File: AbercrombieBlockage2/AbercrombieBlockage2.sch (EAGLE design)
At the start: 35 parts, among them U1 DMN3135LVT, U2 ICS-43434, U3 CYBLE-022001-00, U4 LIS3DH, U5 VL53L0X, U6 VL53L0X, U7 VL53L0X, U8 M24

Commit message: Starting to change the Abercrombie blockage 2 design.
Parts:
- BAT1: DIGIKEY (none) -> BK-913-ND
- C1: DIGIKEYY (none) -> 490-13250-1-ND
- LED1: DIGIKEY (none) -> 160-2162-1-ND
- SV2: DIGIKEY (none) -> 952-2246-ND
- U8: DIGIKEY 497-6348-1-ND -> 497-6351-1-ND
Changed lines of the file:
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@@
 </classes>
 <parts>
-<part name="C1" library="resistor" deviceset="C-US" device="C1210" value="220u"/>
+<part name="C1" library="resistor" deviceset="C-US" device="C1210" value="220u">
+<attribute name="DIGIKEYY" value="490-13250-1-ND"/>
+</part>
 <part name="U1" library="NicksParts" deviceset="DMN3135LVT" device="">
 <attribute name="DIGIKEY" value="DMN3135LVT-7DICT-ND"/>
@@
 <part name="C4" library="resistor" deviceset="C-US" device="C1210" value="10u"/>
 <part name="C3" library="resistor" deviceset="C-US" device="C0603" value="1u"/>
-<part name="SV2" library="con-lstb" deviceset="MA05-1" device=""/>
-<part name="LED1" library="NicksParts" deviceset="LTST-C19HE1WT" device=""/>
+<part name="SV2" library="con-lstb" deviceset="MA05-1" device="">
+<attribute name="DIGIKEY" value="952-2246-ND"/>
+</part>
+<part name="LED1" library="NicksParts" deviceset="LTST-C19HE1WT" device="">
+<attribute name="DIGIKEY" value="160-2162-1-ND"/>
+</part>
 <part name="R2" library="resistor" deviceset="R-US_" device="R0603" value="360"/>
 <part name="U3" library="NicksParts" deviceset="CYBLE-022001-00" device="">
@@
 </part>
 <part name="U8" library="NicksParts" deviceset="M24" device="">
-<attribute name="DIGIKEY" value="497-6348-1-ND"/>
+<attribute name="DIGIKEY" value="497-6351-1-ND"/>
 </part>
 <part name="U4" library="NicksParts" deviceset="LIS3DH" device="">
@@
 <part name="SUPPLY13" library="supply2" deviceset="V+" device=""/>
 <part name="R5" library="resistor" deviceset="R-US_" device="R0603" value="360"/>
-<part name="BAT1" library="NicksParts" deviceset="SN2032" device=""/>
+<part name="BAT1" library="NicksParts" deviceset="SN2032" device="">
+<attribute name="DIGIKEY" value="BK-913-ND"/>
+</part>
 <part name="TX" library="testpad" deviceset="TP" device="B1,27"/>
 <part name="GND" library="testpad" deviceset="TP" device="B1,27"/>
@@
 </plain>
 <instances>
-<instance part="C1" gate="G$1" x="17.78" y="71.12"/>
+<instance part="C1" gate="G$1" x="17.78" y="71.12">
+<attribute name="DIGIKEYY" x="17.78" y="71.12" size="1.778" layer="96" display="off"/>
+</instance>
 <instance part="U1" gate="G$1" x="20.32" y="17.78">
 <attribute name="DIGIKEY" x="20.32" y="17.78" size="1.778" layer="96" display="off"/>
@@
 <instance part="C4" gate="G$1" x="40.64" y="71.12"/>
 <instance part="C3" gate="G$1" x="30.48" y="71.12"/>
-<instance part="SV2" gate="G$1" x="-10.16" y="106.68"/>
-<instance part="LED1" gate="G$1" x="106.68" y="25.4"/>
+<instance part="SV2" gate="G$1" x="-10.16" y="106.68">
+<attribute name="DIGIKEY" x="-10.16" y="106.68" size="1.778" layer="96" display="off"/>
+</instance>
+<instance part="LED1" gate="G$1" x="106.68" y="25.4">
+<attribute name="DIGIKEY" x="106.68" y="25.4" size="1.778" layer="96" display="off"/>
+</instance>
 <instance part="R2" gate="G$1" x="111.76" y="10.16" rot="R270"/>
 <instance part="U3" gate="G$1" x="99.06" y="96.52">
@@
 <instance part="SUPPLY13" gate="1" x="101.6" y="35.56"/>
 <instance part="R5" gate="G$1" x="106.68" y="10.16" rot="R270"/>
-<instance part="BAT1" gate="1" x="0" y="63.5" rot="R90"/>
+<instance part="BAT1" gate="1" x="0" y="63.5" rot="R90">
+<attribute name="DIGIKEY" x="0" y="63.5" size="1.778" layer="96" rot="R90" display="off"/>
+</instance>
 <instance part="TX" gate="G$1" x="-2.54" y="132.08"/>
 <instance part="GND" gate="G$1" x="-7.62" y="129.54"/>

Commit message: Updated some issues with the Abercrombie Gen4 spray system. Completely re-routed the design.
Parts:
- removed BAT1: (no value), NicksParts:SN2032
- removed U1: DMN3135LVT, NicksParts:DMN3135LVT
- added B1: (no value), NicksParts:BU2032
- added SCL, SDA: TPB1,27, testpad:TPB1,27
- added U9: (no value), NicksParts:TPS22929D
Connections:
- net GND: now also B1.-, U9.GND, U9.GND2; no longer BAT1.-
- net PWR_EN: now also U9.ON; no longer U1.G1, U1.G2
- net SCL: now also SCL.TP
- net SDA: now also SDA.TP
- net V+: now also U9.VOUT; no longer U1.S1
- net VDD: now also B1.+, U9.VIN, U9.VIN2; no longer BAT1.+, U1.D1

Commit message: Minor updates to the layout.
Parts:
- C4: value 10u -> 220u
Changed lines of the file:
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@@
 <part name="SV1" library="con-lstb" deviceset="MA03-1" device=""/>
 <part name="GND2" library="supply1" deviceset="GND" device=""/>
-<part name="C4" library="resistor" deviceset="C-US" device="C1210" value="10u"/>
+<part name="C4" library="resistor" deviceset="C-US" device="C1210" value="220u"/>
 <part name="C3" library="resistor" deviceset="C-US" device="C0603" value="1u"/>
 <part name="SV2" library="con-lstb" deviceset="MA05-1" device="">

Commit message: Order V2 of the Gen4 spray pattern monitor.
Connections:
- net GND: no longer U8.A0
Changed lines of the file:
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@@
 <grid distance="0.1" unitdist="inch" unit="inch" style="lines" multiple="1" display="no" altdistance="0.01" altunitdist="inch" altunit="inch"/>
 <layers>
-<layer number="1" name="Top" color="4" fill="1" visible="yes" active="no"/>
-<layer number="16" name="Bottom" color="1" fill="1" visible="yes" active="no"/>
-<layer number="17" name="Pads" color="2" fill="1" visible="yes" active="no"/>
-<layer number="18" name="Vias" color="2" fill="1" visible="yes" active="no"/>
-<layer number="19" name="Unrouted" color="6" fill="1" visible="yes" active="no"/>
-<layer number="20" name="Dimension" color="15" fill="1" visible="yes" active="no"/>
-<layer number="21" name="tPlace" color="16" fill="1" visible="yes" active="no"/>
-<layer number="22" name="bPlace" color="14" fill="1" visible="yes" active="no"/>
-<layer number="23" name="tOrigins" color="15" fill="1" visible="yes" active="no"/>
-<layer number="24" name="bOrigins" color="15" fill="1" visible="yes" active="no"/>
-<layer number="25" name="tNames" color="7" fill="1" visible="yes" active="no"/>
-<layer number="26" name="bNames" color="7" fill="1" visible="yes" active="no"/>
-<layer number="27" name="tValues" color="7" fill="1" visible="yes" active="no"/>
-<layer number="28" name="bValues" color="7" fill="1" visible="yes" active="no"/>
+<layer number="1" name="Top" color="4" fill="1" visible="no" active="no"/>
+<layer number="16" name="Bottom" color="1" fill="1" visible="no" active="no"/>
+<layer number="17" name="Pads" color="2" fill="1" visible="no" active="no"/>
+<layer number="18" name="Vias" color="2" fill="1" visible="no" active="no"/>
+<layer number="19" name="Unrouted" color="6" fill="1" visible="no" active="no"/>
+<layer number="20" name="Dimension" color="15" fill="1" visible="no" active="no"/>
+<layer number="21" name="tPlace" color="16" fill="1" visible="no" active="no"/>
+<layer number="22" name="bPlace" color="14" fill="1" visible="no" active="no"/>
+<layer number="23" name="tOrigins" color="15" fill="1" visible="no" active="no"/>
+<layer number="24" name="bOrigins" color="15" fill="1" visible="no" active="no"/>
+<layer number="25" name="tNames" color="7" fill="1" visible="no" active="no"/>
+<layer number="26" name="bNames" color="7" fill="1" visible="no" active="no"/>
+<layer number="27" name="tValues" color="7" fill="1" visible="no" active="no"/>
+<layer number="28" name="bValues" color="7" fill="1" visible="no" active="no"/>
 <layer number="29" name="tStop" color="7" fill="3" visible="no" active="no"/>
 <layer number="30" name="bStop" color="7" fill="6" visible="no" active="no"/>
@@
 <layer number="35" name="tGlue" color="7" fill="4" visible="no" active="no"/>
 <layer number="36" name="bGlue" color="7" fill="5" visible="no" active="no"/>
-<layer number="37" name="tTest" color="7" fill="1" visible="yes" active="no"/>
-<layer number="38" name="bTest" color="7" fill="1" visible="yes" active="no"/>
+<layer number="37" name="tTest" color="7" fill="1" visible="no" active="no"/>
+<layer number="38" name="bTest" color="7" fill="1" visible="no" active="no"/>
 <layer number="39" name="tKeepout" color="4" fill="11" visible="no" active="no"/>
 <layer number="40" name="bKeepout" color="1" fill="11" visible="no" active="no"/>
@@
 <layer number="44" name="Drills" color="7" fill="1" visible="no" active="no"/>
 <layer number="45" name="Holes" color="7" fill="1" visible="no" active="no"/>
-<layer number="46" name="Milling" color="3" fill="1" visible="yes" active="no"/>
-<layer number="47" name="Measures" color="7" fill="1" visible="yes" active="no"/>
-<layer number="48" name="Document" color="7" fill="1" visible="yes" active="no"/>
-<layer number="49" name="Reference" color="7" fill="1" visible="yes" active="no"/>
-<layer number="51" name="tDocu" color="6" fill="1" visible="yes" active="no"/>
-<layer number="52" name="bDocu" color="7" fill="1" visible="yes" active="no"/>
+<layer number="46" name="Milling" color="3" fill="1" visible="no" active="no"/>
+<layer number="47" name="Measures" color="7" fill="1" visible="no" active="no"/>
+<layer number="48" name="Document" color="7" fill="1" visible="no" active="no"/>
+<layer number="49" name="Reference" color="7" fill="1" visible="no" active="no"/>
+<layer number="51" name="tDocu" color="6" fill="1" visible="no" active="no"/>
+<layer number="52" name="bDocu" color="7" fill="1" visible="no" active="no"/>
 <layer number="90" name="Modules" color="5" fill="1" visible="yes" active="yes"/>
 <layer number="91" name="Nets" color="2" fill="1" visible="yes" active="yes"/>
@@
 </segment>
 <segment>
-<pinref part="U8" gate="G$1" pin="A0"/>
 <pinref part="GND7" gate="1" pin="GND"/>
-<wire x1="187.96" y1="-5.08" x2="182.88" y2="-5.08" width="0.1524" layer="91"/>
-<wire x1="182.88" y1="-5.08" x2="182.88" y2="-7.62" width="0.1524" layer="91"/>
 <pinref part="U8" gate="G$1" pin="A1"/>
 <wire x1="182.88" y1="-7.62" x2="182.88" y2="-10.16" width="0.1524" layer="91"/>
@@
 <pinref part="U8" gate="G$1" pin="WC"/>
 <wire x1="187.96" y1="0" x2="182.88" y2="0" width="0.1524" layer="91"/>
-<wire x1="182.88" y1="0" x2="182.88" y2="-5.08" width="0.1524" layer="91"/>
-<junction x="182.88" y="-5.08"/>
-</segment>
-<segment>
+<wire x1="182.88" y1="0" x2="182.88" y2="-7.62" width="0.1524" layer="91"/>
+</segment>
+<segment>

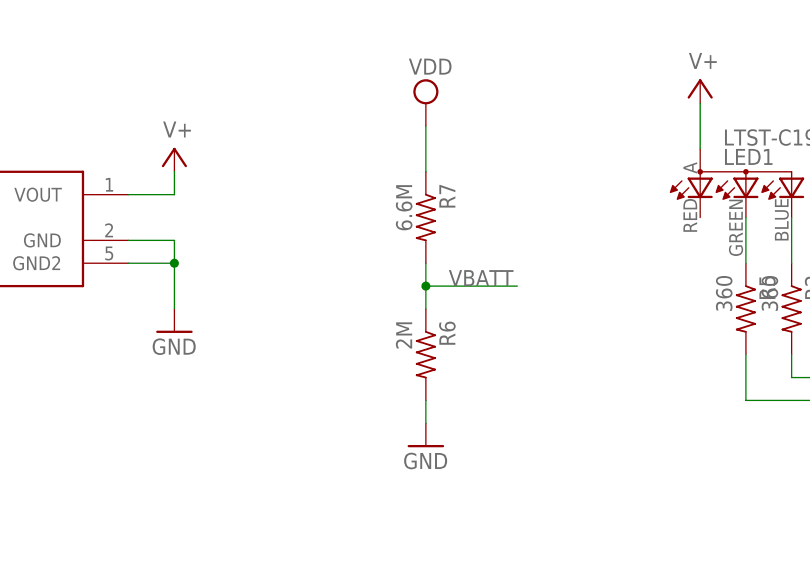
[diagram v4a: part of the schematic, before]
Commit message: Added a readme indicated the Abercrombie projects have been moved.
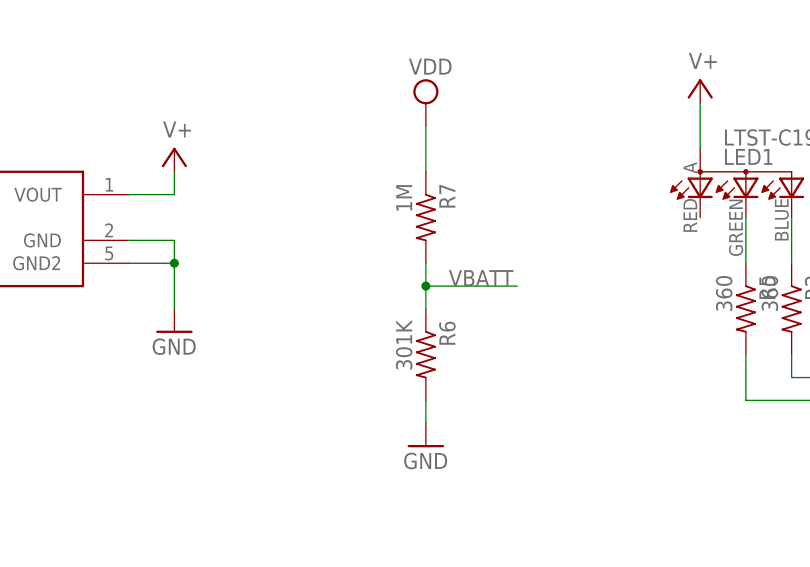
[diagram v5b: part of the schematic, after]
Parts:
- R6: value 2M -> 301K
- R7: value 6.6M -> 1M
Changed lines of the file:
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@@
 <part name="TX" library="testpad" deviceset="TP" device="B1,27"/>
 <part name="GND" library="testpad" deviceset="TP" device="B1,27"/>
-<part name="R6" library="resistor" deviceset="R-US_" device="R0603" value="2M"/>
-<part name="R7" library="resistor" deviceset="R-US_" device="R0603" value="6.6M"/>
+<part name="R6" library="resistor" deviceset="R-US_" device="R0603" value="301K"/>
+<part name="R7" library="resistor" deviceset="R-US_" device="R0603" value="1M"/>
 <part name="GND4" library="supply1" deviceset="GND" device=""/>
 <part name="SUPPLY14" library="supply2" deviceset="VDD" device=""/>
